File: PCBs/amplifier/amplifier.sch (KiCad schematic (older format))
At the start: 98 parts, among them J1 6V3A, J2 6V3B, J3 AUX-IN, J4 AUX-IN-GND, J5 +38V, J6 -38V, J7 GND, J8 +310V, P1 2k, P2 5k, P3 5k, Q1 BD139, Q10 BC547, Q2 2SC2073, Q3 2SA940, Q4 2SC5200, Q5 2SC5200, Q6 BC550, Q7 BC550, Q8 BS170, Q9 BC547, U1 LM337, U2 LM317

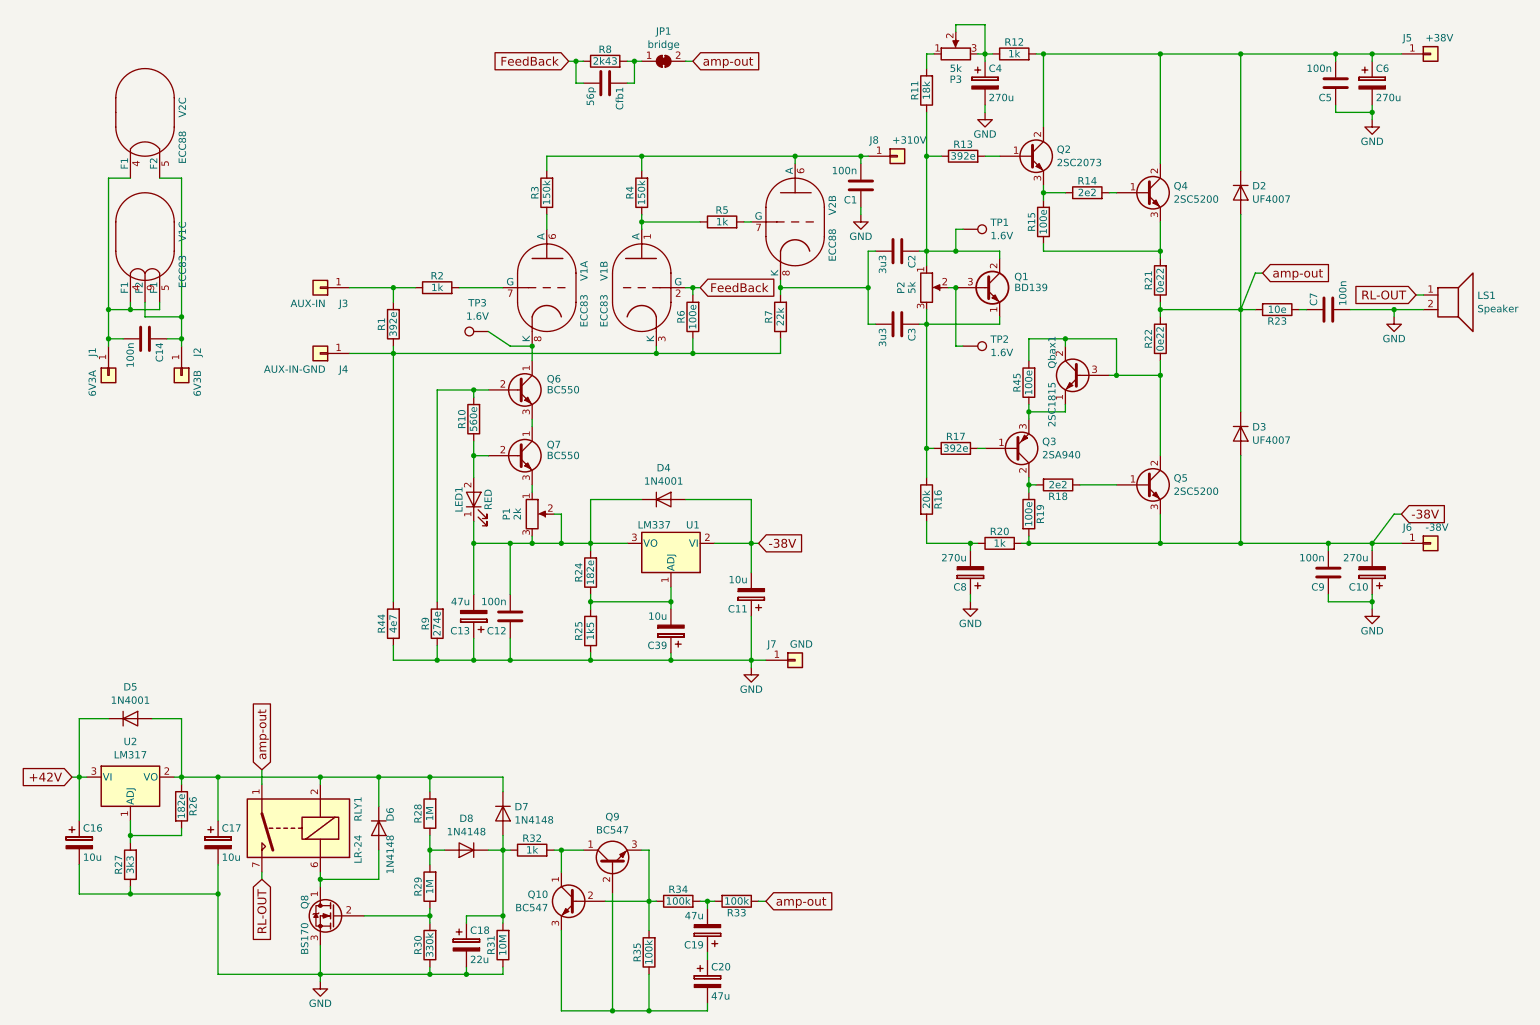
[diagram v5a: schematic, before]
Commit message: amp. sch. done, all footprints added.
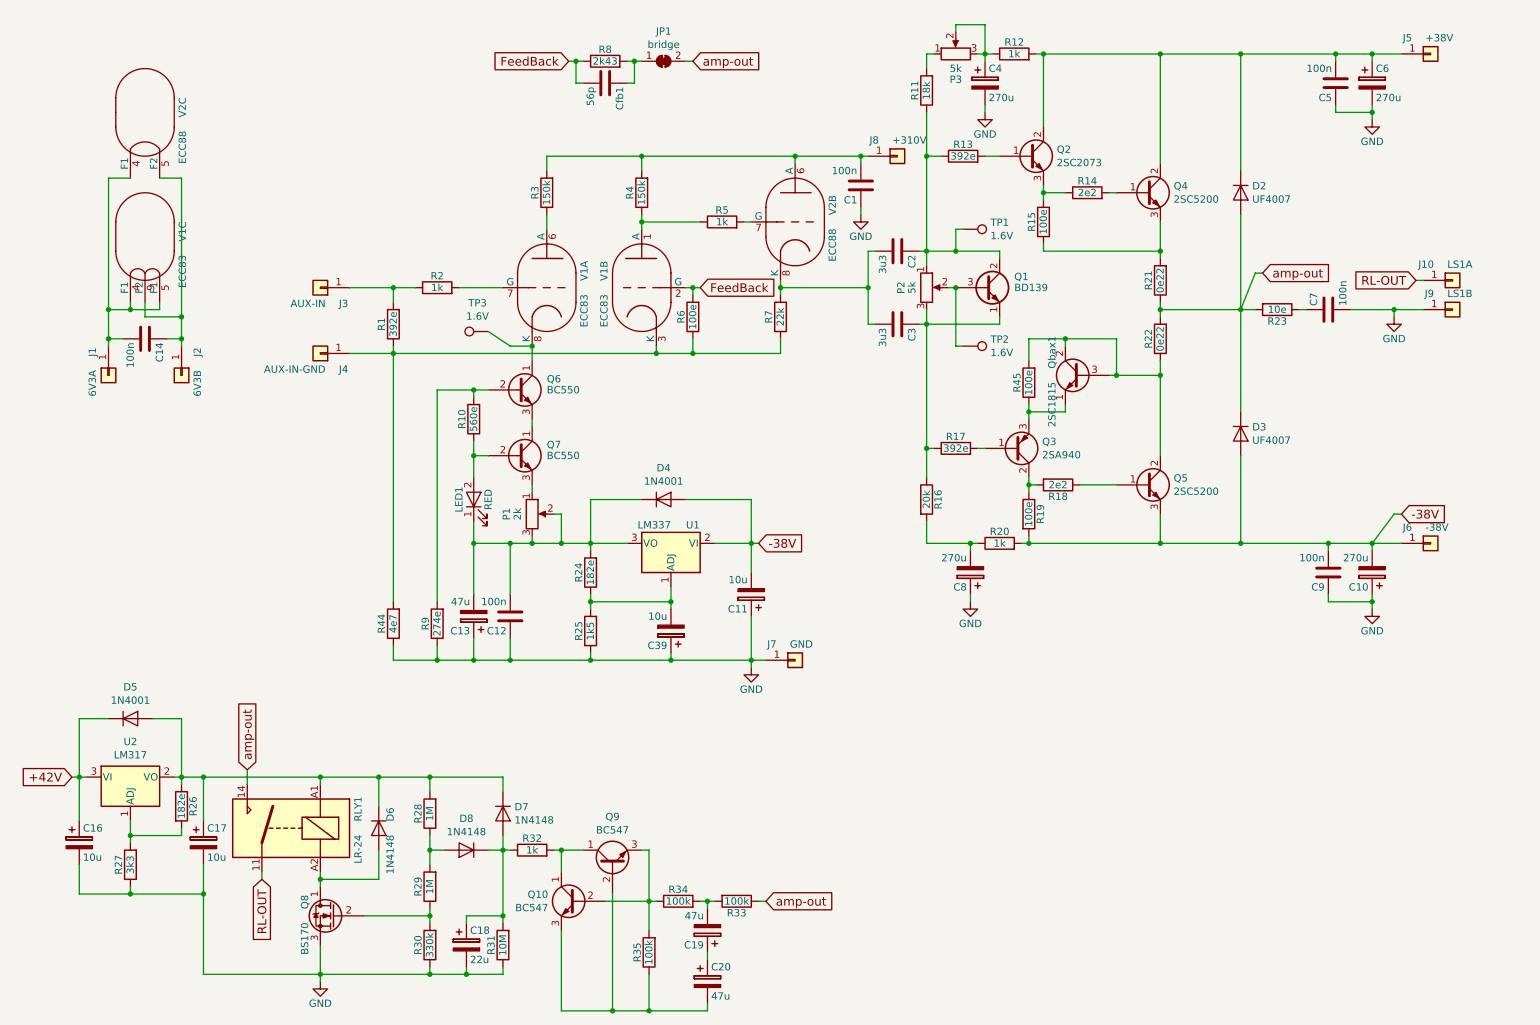
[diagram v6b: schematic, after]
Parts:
- removed LS1: Speaker, symbol Device:Speaker
- removed RLY1: LR-24, Relay_THT:Relay_StandexMeder_DIP_LowProfile, symbol Relay:DIPxx-1Axx-11x
- added J10: LS1A, Connector_Wire:SolderWirePad_single_2mmDrill, symbol Connector_Generic:Conn_01x01
- added J9: LS1B, Connector_Wire:SolderWirePad_single_2mmDrill, symbol Connector_Generic:Conn_01x01
- added RLY1: LR-24, Relay_THT:Relay_SPST_Schrack-RP-II-1-16A-FormA_RM5mm, symbol Relay:RM50-xx21
- C1: footprint (none) -> Capacitor_THT:C_Rect_L16.5mm_W6.0mm_P15.00mm_MKT
- C10, C4, C6, C8: footprint (none) -> Capacitor_THT:CP_Radial_D10.0mm_P3.80mm
- C11, C16, C17, C18: footprint (none) -> Capacitor_THT:CP_Radial_D6.3mm_P2.50mm
- C12, C14, C5, C9: footprint (none) -> Capacitor_THT:C_Rect_L9.0mm_W3.8mm_P7.50mm_MKT
- C13, C19, C20: footprint (none) -> Capacitor_THT:CP_Radial_D10.0mm_P5.00mm
- C2, C3: footprint (none) -> Capacitor_THT:C_Rect_L41.5mm_W24.0mm_P37.50mm_MKS4
- C39: footprint (none) -> Capacitor_THT:CP_Radial_D5.0mm_P2.00mm
- C7: footprint (none) -> Capacitor_THT:C_Rect_L7.2mm_W5.5mm_P5.00mm_FKS2_FKP2_MKS2_MKP2
- Cfb1: footprint (none) -> Capacitor_THT:C_Disc_D5.0mm_W2.5mm_P2.50mm
- D2: footprint TestPoint:TestPoint_Pad_D1.0mm -> Diode_THT:D_DO-41_SOD81_P10.16mm_Horizontal
- J1, J2, J3, J4, J5, J6, J7, J8: footprint (none) -> Connector_Wire:SolderWirePad_single_2mmDrill
- JP1: footprint (none) -> Jumper:SolderJumper-2_P1.3mm_Bridged_RoundedPad1.0x1.5mm
- LED1: footprint (none) -> LED_THT:LED_D3.0mm
- Q1: footprint TO_SOT_Packages_THT:TO-126_Vertical -> Package_TO_SOT_THT:TO-126_Vertical
- Q10, Q9, Qbax1: footprint Package_TO_SOT_THT:TO-92_Inline -> Package_TO_SOT_THT:TO-92
- Q2, Q3: footprint (none) -> Package_TO_SOT_THT:TO-220-3_Vertical
- Q6, Q7: footprint TO_SOT_Packages_THT:TO-92_Molded_Narrow -> Package_TO_SOT_THT:TO-92
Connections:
- net GND: now also J9.1 (Pin_1)
- net RL-OUT: now also J10.1 (Pin_1), RLY1.11
- net amp-out: now also RLY1.14
- net at C17.1, D5.2 (A), D6.1 (K)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: now also RLY1.A1
- net at D6.2 (A), Q8.1 (D): now also RLY1.A2
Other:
- moved on the sheet: C17

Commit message: Rough component placement amp. pcb.
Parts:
- P1, P2, P3: footprint Potentiometer_THT:Potentiometer_ACP_CA14-H2,5_Horizontal -> Potentiometer_THT:Potentiometer_Bourns_3266Y_Vertical
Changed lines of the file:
@@
 F 0 "P1" V 4125 4000 50  0000 C CNN
 F 1 "2k" V 4200 4000 50  0000 C CNN
-F 2 "Potentiometer_THT:Potentiometer_ACP_CA14-H2,5_Horizontal" H 4300 4000 50  0001 C CNN
+F 2 "Potentiometer_THT:Potentiometer_Bourns_3266Y_Vertical" H 4300 4000 50  0001 C CNN
 F 3 "" H 4300 4000 50  0001 C CNN
 	1    4300 4000
@@
 F 0 "P2" V 6825 2450 50  0000 C CNN
 F 1 "5k" V 6900 2450 50  0000 C CNN
-F 2 "Potentiometer_THT:Potentiometer_ACP_CA14-H2,5_Horizontal" H 7000 2450 50  0001 C CNN
+F 2 "Potentiometer_THT:Potentiometer_Bourns_3266Y_Vertical" H 7000 2450 50  0001 C CNN
 F 3 "" H 7000 2450 50  0001 C CNN
 	1    7000 2450
@@
 F 0 "P3" V 7025 850 50  0000 C CNN
 F 1 "5k" V 7100 850 50  0000 C CNN
-F 2 "Potentiometer_THT:Potentiometer_ACP_CA14-H2,5_Horizontal" H 7200 850 50  0001 C CNN
+F 2 "Potentiometer_THT:Potentiometer_Bourns_3266Y_Vertical" H 7200 850 50  0001 C CNN
 F 3 "" H 7200 850 50  0001 C CNN
 	1    7200 850
